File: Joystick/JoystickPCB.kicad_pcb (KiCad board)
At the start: 2 copper layers, 62 x 42 mm, 21 parts, among them J1 JST B6B-PH-SM4-TB, J2 JST B4B-PH-SM4-TB, J3 JST B4B-PH-SM4-TB, J4 JST B3B-PH-SM4-TB, U1 MIC5225-1.8YM5-TR, U2 ADS1115IDGSR, U3 ICM-20948

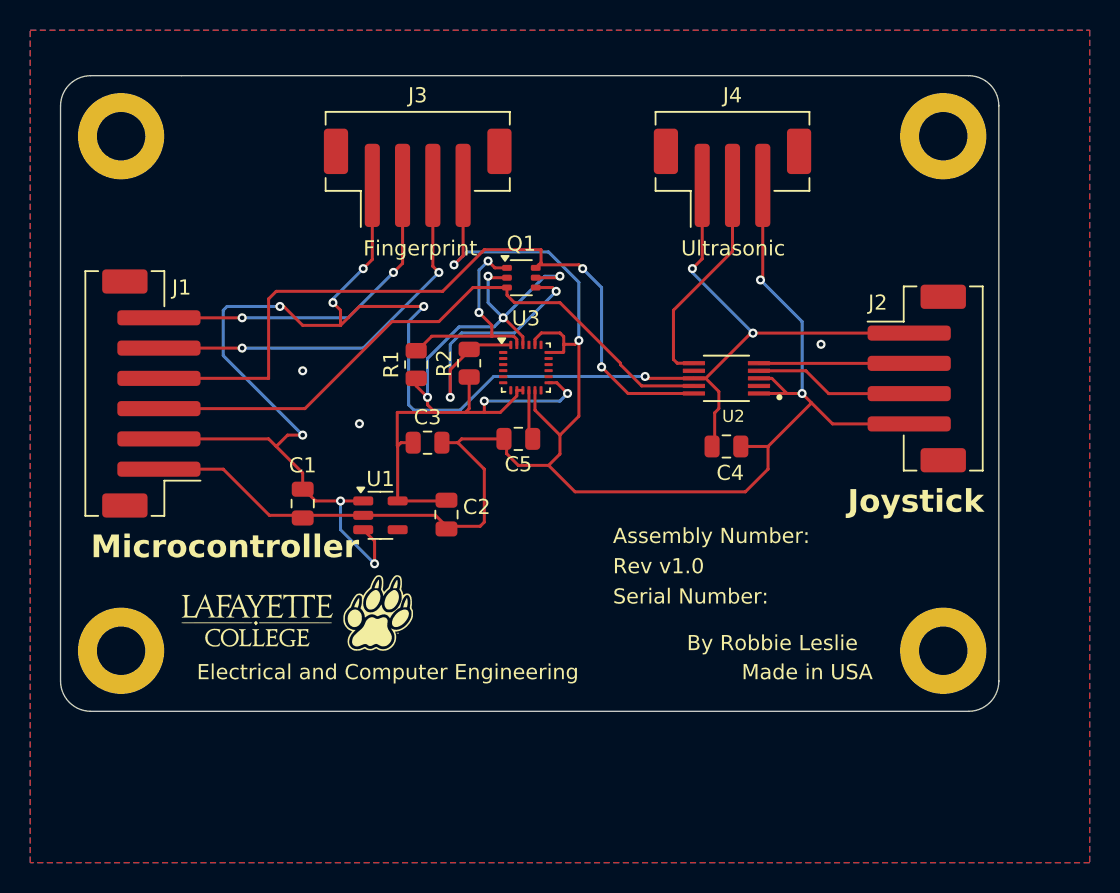
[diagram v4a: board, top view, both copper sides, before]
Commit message: Fixed mounting holes positions and general board cleanup
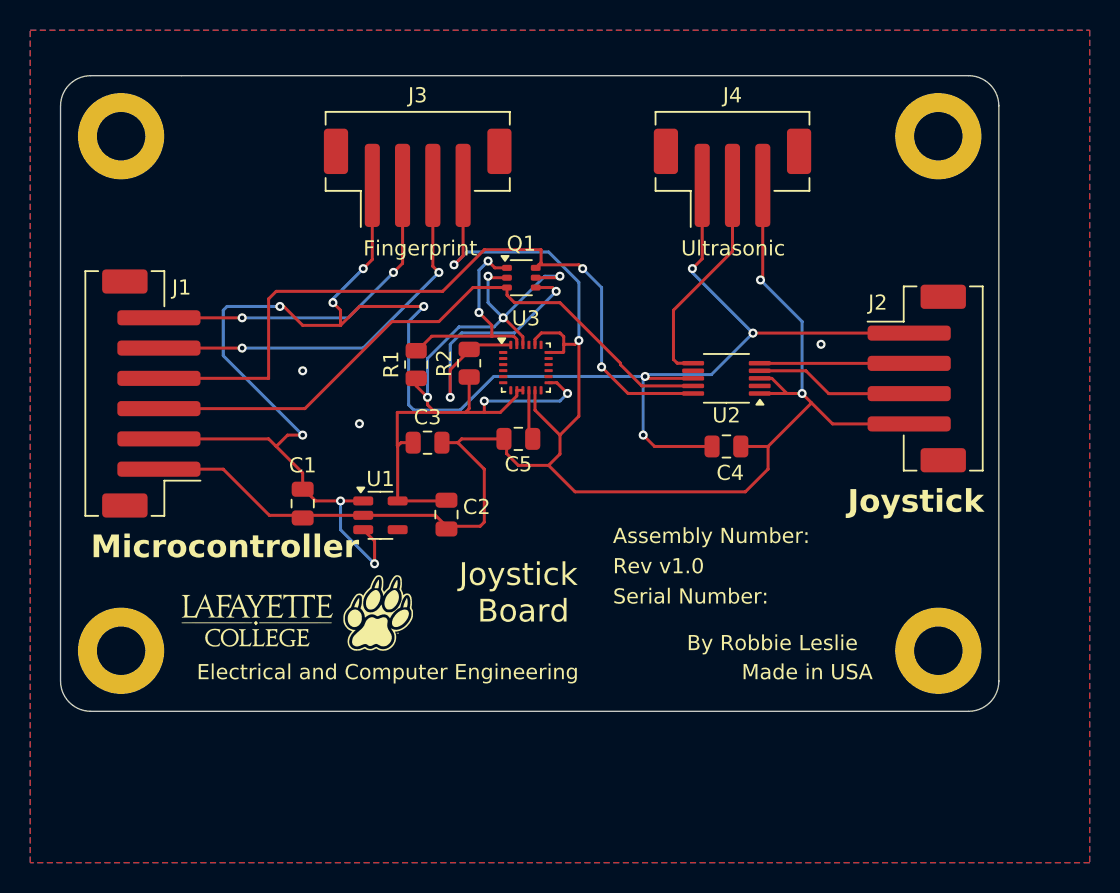
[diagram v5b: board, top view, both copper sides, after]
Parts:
- U2: footprint Library:SOP50P490X110-10N -> Package_SO:VSSOP-10_3x3mm_P0.5mm
- moved H2 0.32 mm to (184.0, 51.0)
- moved H4 0.32 mm to (184.0, 85.0)
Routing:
- net /3.3V: track 120.2 -> 127.3 mm, vias 10 -> 11
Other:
- board text added: "Joystick Board"
- board text removed: "Might need to modify board size, although that will also proably change with the new connector"

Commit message: Swapped microcontroller connector for horizontal one
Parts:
- J1: footprint Connector_JST:JST_PH_B6B-PH-SM4-TB_1x06-1MP_P2.00mm_Vertical -> Connector_JST:JST_PH_S6B-PH-SM4-TB_1x06-1MP_P2.00mm_Horizontal
- moved J1 0.10 mm to (131.9, 68.0), turned to -90 degrees
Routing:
- net /GND: track 126.3 -> 117.7 mm, vias 7 -> 9
- net /3.3V: track 127.3 -> 120.7 mm, vias 11 -> 12
- net /TX: track 22.7 -> 28.1 mm
- net /RX: track 26.5 -> 29.5 mm
- net /SDA: track 41.7 -> 39.1 mm, vias 0 -> 2
- net /SCL: track 50.3 -> 49.0 mm
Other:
- board text removed: "1.0"
- board text removed: "2/2/25"
- board text removed: "Joystick ADC + IMU Breakout Board"

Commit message: Added board part number
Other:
- board text added: "Board Part Number: 2"
- board text removed: "Board Part Number:"
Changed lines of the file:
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@@
 		)
 	)
-	(gr_text "Board Part Number: "
+	(gr_text "Board Part Number: 2"
 		(at 187 77 0)
 		(layer "B.SilkS")

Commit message: Updated ultrasonic header connection to match with sensor pinout
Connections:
- J4 pad 1: /3.3V -> /A2
- J4 pad 2: /A2 -> /3.3V
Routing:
- net /3.3V: track 120.7 -> 119.3 mm
- net /A2: track 14.6 -> 13.7 mm
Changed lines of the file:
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@@
 			(size 5.7 5.7)
 			(drill 3.2)
-			(layers "*.Cu" "*.Mask")
+			(layers "*.Cu" "*.Mask" "In1.Cu" "In2.Cu" "In3.Cu" "In4.Cu" "In5.Cu" "In6.Cu"
+				"In7.Cu" "In8.Cu" "In9.Cu" "In10.Cu" "In11.Cu" "In12.Cu" "In13.Cu" "In14.Cu"
+				"In15.Cu" "In16.Cu" "In17.Cu" "In18.Cu" "In19.Cu" "In20.Cu" "In21.Cu"
+				"In22.Cu" "In23.Cu" "In24.Cu" "In25.Cu" "In26.Cu" "In27.Cu" "In28.Cu"
+				"In29.Cu" "In30.Cu"
+			)
 			(remove_unused_layers no)
 		)
@@
 			(size 5.7 5.7)
 			(drill 3.2)
-			(layers "*.Cu" "*.Mask")
+			(layers "*.Cu" "*.Mask" "In1.Cu" "In2.Cu" "In3.Cu" "In4.Cu" "In5.Cu" "In6.Cu"
+				"In7.Cu" "In8.Cu" "In9.Cu" "In10.Cu" "In11.Cu" "In12.Cu" "In13.Cu" "In14.Cu"
+				"In15.Cu" "In16.Cu" "In17.Cu" "In18.Cu" "In19.Cu" "In20.Cu" "In21.Cu"
+				"In22.Cu" "In23.Cu" "In24.Cu" "In25.Cu" "In26.Cu" "In27.Cu" "In28.Cu"
+				"In29.Cu" "In30.Cu"
+			)
 			(remove_unused_layers no)
 		)
@@
 			(size 5.7 5.7)
 			(drill 3.2)
-			(layers "*.Cu" "*.Mask")
+			(layers "*.Cu" "*.Mask" "In1.Cu" "In2.Cu" "In3.Cu" "In4.Cu" "In5.Cu" "In6.Cu"
+				"In7.Cu" "In8.Cu" "In9.Cu" "In10.Cu" "In11.Cu" "In12.Cu" "In13.Cu" "In14.Cu"
+				"In15.Cu" "In16.Cu" "In17.Cu" "In18.Cu" "In19.Cu" "In20.Cu" "In21.Cu"
+				"In22.Cu" "In23.Cu" "In24.Cu" "In25.Cu" "In26.Cu" "In27.Cu" "In28.Cu"
+				"In29.Cu" "In30.Cu"
+			)
 			(remove_unused_layers no)
 		)
@@
 			(layers "F.Cu" "F.Paste" "F.Mask")
 			(roundrect_rratio 0.25)
-			(net 9 "/3.3V")
+			(net 6 "/A2")
 			(pinfunction "Pin_1")
 			(pintype "passive")
@@
 			(layers "F.Cu" "F.Paste" "F.Mask")
 			(roundrect_rratio 0.25)
-			(net 6 "/A2")
+			(net 9 "/3.3V")
 			(pinfunction "Pin_2")
 			(pintype "passive")
@@
 			(size 5.7 5.7)
 			(drill 3.2)
-			(layers "*.Cu" "*.Mask")
+			(layers "*.Cu" "*.Mask" "In1.Cu" "In2.Cu" "In3.Cu" "In4.Cu" "In5.Cu" "In6.Cu"
+				"In7.Cu" "In8.Cu" "In9.Cu" "In10.Cu" "In11.Cu" "In12.Cu" "In13.Cu" "In14.Cu"
+				"In15.Cu" "In16.Cu" "In17.Cu" "In18.Cu" "In19.Cu" "In20.Cu" "In21.Cu"
+				"In22.Cu" "In23.Cu" "In24.Cu" "In25.Cu" "In26.Cu" "In27.Cu" "In28.Cu"
+				"In29.Cu" "In30.Cu"
+			)
 			(remove_unused_layers no)
 		)
@@
 	)
 	(segment
-		(start 167.85 66)
-		(end 166.75 66)
+		(start 166.75 66)
+		(end 166.5 65.75)
 		(width 0.2)
 		(layer "F.Cu")
@@
 	)
 	(segment
-		(start 166.5 65.75)
-		(end 166.5 62.5)
+		(start 168.4 60.268)
+		(end 168.4 54.25)
 		(width 0.2)
 		(layer "F.Cu")
@@
 	)
 	(segment
-		(start 166.5 62.5)
-		(end 170.4 58.6)
+		(start 166.5 62.168)
+		(end 168.4 60.268)
 		(width 0.2)
 		(layer "F.Cu")
@@
 	)
 	(segment
-		(start 170.4 58.6)
-		(end 170.4 54.25)
+		(start 166.5 65.75)
+		(end 166.5 62.168)
 		(width 0.2)
 		(layer "F.Cu")
@@
 	)
 	(segment
-		(start 166.75 66)
-		(end 166.5 65.75)
+		(start 167.85 66)
+		(end 166.75 66)
 		(width 0.2)
 		(layer "F.Cu")
@@
 	)
 	(segment
+		(start 170.4 59.628)
+		(end 170.482 59.71)
+		(width 0.2)
+		(layer "F.Cu")
+		(net 9)
+	)
+	(segment
 		(start 171.75 64.01)
 		(end 171.619732 64.01)
@@
 	)
 	(segment
-		(start 168.4 54.25)
-		(end 168.4 59.1)
-		(width 0.2)
-		(layer "F.Cu")
-		(net 9)
-	)
-	(segment
 		(start 138.5 64.5)
 		(end 138 65)
@@
 	)
 	(segment
+		(start 170.4 54.25)
+		(end 170.4 59.628)
+		(width 0.2)
+		(layer "F.Cu")
+		(net 9)
+	)
+	(segment
 		(start 145.75 62.25)
 		(end 144.5 63.5)
@@
 	)
 	(segment
-		(start 168.4 59.1)
-		(end 167.75 59.75)
-		(width 0.2)
-		(layer "F.Cu")
-		(net 9)
-	)
-	(segment
 		(start 144.5 75.1)
 		(end 146 75.1)
@@
 	)
 	(via
-		(at 167.75 59.75)
+		(at 170.482 59.71)
 		(size 0.6)
 		(drill 0.3)
@@
 	)
 	(segment
+		(start 170.482 59.71)
+		(end 170.482 62.742)
+		(width 0.2)
+		(layer "B.Cu")
+		(net 9)
+	)
+	(segment
 		(start 144 61.75)
 		(end 144 62)
@@
 	)
 	(segment
-		(start 140.5 63.5)
-		(end 138.5 63.5)
+		(start 170.482 62.742)
+		(end 171.75 64.01)
 		(width 0.2)
 		(layer "B.Cu")
@@
 	)
 	(segment
-		(start 167.75 59.75)
-		(end 167.75 60.01)
+		(start 140.5 63.5)
+		(end 138.5 63.5)
 		(width 0.2)
 		(layer "B.Cu")
@@
 	)
 	(segment
-		(start 167.75 60.01)
-		(end 171.75 64.01)
-		(width 0.2)
-		(layer "B.Cu")
-		(net 9)
-	)
-	(segment
 		(start 146.75 79.25)
 		(end 144.5 77)
@@
 		(net 7)
 		(net_name "/GND")
-		(layers "F&B.Cu")
+		(layers "F.Cu" "B.Cu")
 		(hatch edge 0.5)
 		(connect_pads
